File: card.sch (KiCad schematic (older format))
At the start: 25 parts, among them J1 Conn_02x03_Odd_Even, P2_FPC24/0.5MM1 Conn_01x24_Male, Q1 Si1308EDL, U1 ATMEGA168PA-AU

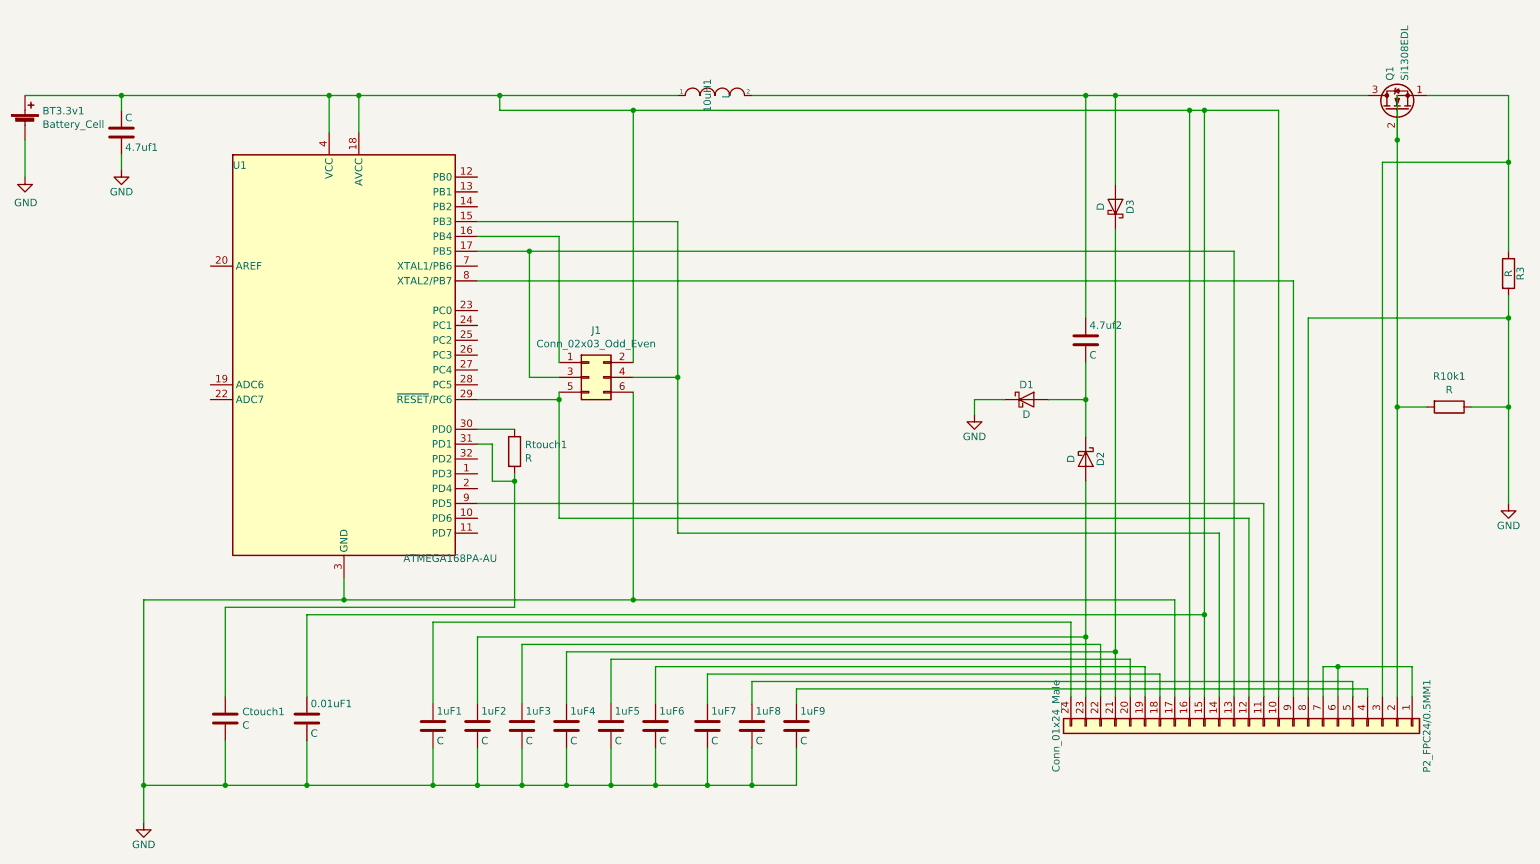
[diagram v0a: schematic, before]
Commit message: fixed FPC connector footprint, updated traces
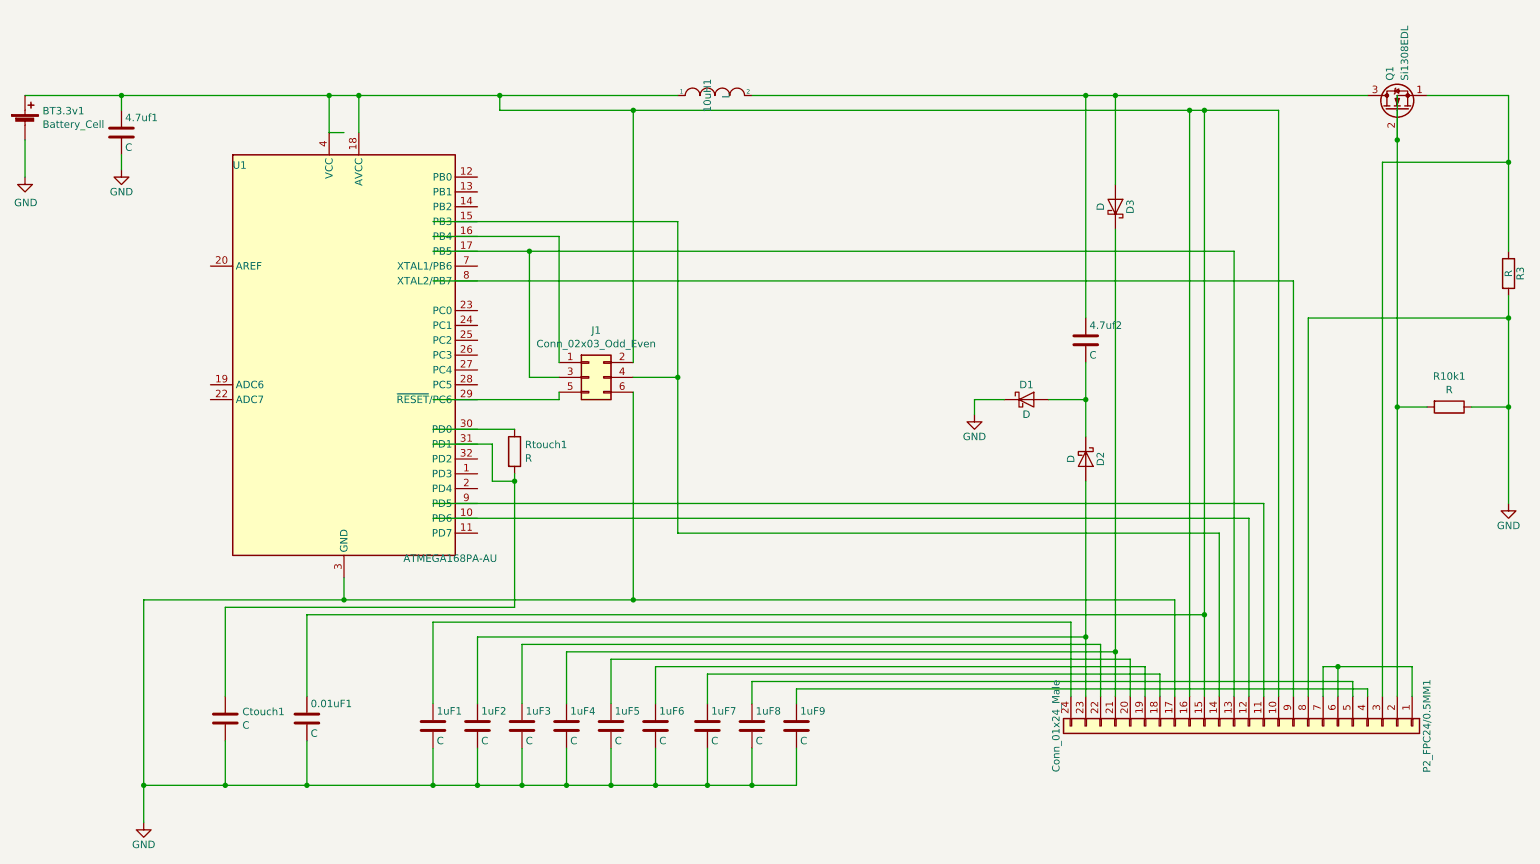
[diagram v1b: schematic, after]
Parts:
- C: renamed from 4.7uf1; value C -> 4.7uf1
- P2_FPC24/0.5MM1: footprint Connectors_FPC:Hirose_FH12-24S-0.5SH_1x24_P0.50mm_Horizontal_Gnd17 -> Connectors_FPC:Hirose_FH12-24S-0.5SH_1x24_P0.50mm_Horizontal_Gnd17_Mirr
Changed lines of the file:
@@
 F 0 "P2_FPC24/0.5MM1" H 8950 7050 50  0000 C CNN
 F 1 "Conn_01x24_Male" H 8950 4550 50  0000 C CNN
-F 2 "Connectors_FPC:Hirose_FH12-24S-0.5SH_1x24_P0.50mm_Horizontal_Gnd17" H 8950 5850 50  0001 C CNN
+F 2 "Connectors_FPC:Hirose_FH12-24S-0.5SH_1x24_P0.50mm_Horizontal_Gnd17_Mirr" H 8950 5850 50  0001 C CNN
 F 3 "" H 8950 5850 50  0001 C CNN
 	1    8950 5850
@@
 $EndComp
 $Comp
-L Device:C 4.7uf1
+L Device:C C
 U 1 1 5AB85D32
 P 1350 1850
-F 0 "4.7uf1" H 1375 1950 50  0000 L CNN
-F 1 "C" H 1375 1750 50  0000 L CNN
+F 0 "C" H 1375 1950 50  0000 L CNN
+F 1 "4.7uf1" H 1375 1750 50  0000 L CNN
 F 2 "Capacitors_SMD:C_0402" H 1388 1700 50  0001 C CNN
 F 3 "" H 1350 1850 50  0001 C CNN
@@
 	3900 1600 5100 1600
 Wire Wire Line
-	3750 2850 9250 2850
-Wire Wire Line
-	3750 4350 9050 4350
-Wire Wire Line
 	9950 1600 9950 1900
 Connection ~ 9950 1900
@@
 	4300 3600 4300 3650
 Wire Wire Line
-	4300 3650 3750 3650
-Wire Wire Line
 	4300 3400 4300 2550
 Wire Wire Line
-	4300 2550 3750 2550
-Wire Wire Line
-	3750 2450 5100 2450
-Wire Wire Line
 	5100 2450 5100 3500
 Wire Wire Line
@@
 Wire Wire Line
 	4100 3500 4100 2650
-Wire Wire Line
-	4100 2650 3750 2650
 Wire Wire Line
 	2950 1850 2950 1600
@@
 	4000 4150 4000 4200
 Wire Wire Line
-	3750 3950 3850 3950
-Wire Wire Line
 	3850 3950 3850 4200
 Wire Wire Line
@@
 	4000 4200 4000 5050
 Wire Wire Line
-	4000 3850 3750 3850
-Wire Wire Line
-	4300 3650 4300 4450
-Connection ~ 4300 3650
-Wire Wire Line
-	4300 4450 8950 4450
-Wire Wire Line
 	5100 3500 5100 4550
 Connection ~ 5100 3500
@@
 Wire Wire Line
 	4100 2650 8850 2650
+Wire Wire Line
+	2750 1850 2850 1850
+Wire Wire Line
+	3450 2450 5100 2450
+Wire Wire Line
+	3450 2550 4300 2550
+Wire Wire Line
+	3450 2650 4100 2650
+Wire Wire Line
+	3450 2850 9250 2850
+Wire Wire Line
+	3450 3650 4300 3650
+Wire Wire Line
+	3450 3850 4000 3850
+Wire Wire Line
+	3450 3950 3850 3950
+Wire Wire Line
+	3450 4350 9050 4350
+Wire Wire Line
+	3450 4450 8950 4450
 $EndSCHEMATC

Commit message: increased some footprint sizes, added missing via
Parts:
- 0.01uF1, 1uF1, 1uF2, 1uF3, 1uF4, 1uF5, 1uF6, 1uF7, 1uF8, 1uF9, 4.7uf2: footprint Capacitors_SMD:C_0402 -> Capacitors_SMD:C_0603_HandSoldering
- C1: renamed from C; footprint Capacitors_SMD:C_0402 -> Capacitors_SMD:C_0603_HandSoldering
- D1, D2, D3: footprint Diodes_SMD:D_0805 -> Diodes_SMD:D_SOD-123
- R10k1, R3, Rtouch1: footprint Resistors_SMD:R_0402 -> Resistors_SMD:R_0603_HandSoldering
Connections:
- wire segments 141 -> 143
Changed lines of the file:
@@
 F 0 "R3" V 10780 2800 50  0000 C CNN
 F 1 "R" V 10700 2800 50  0000 C CNN
-F 2 "Resistors_SMD:R_0402" V 10630 2800 50  0001 C CNN
+F 2 "Resistors_SMD:R_0603_HandSoldering" V 10630 2800 50  0001 C CNN
 F 3 "" H 10700 2800 50  0001 C CNN
 F 4 "R" H 10700 2800 50  0001 C CNN "Spice_Primitive"
@@
 F 0 "D1" H 7450 3750 50  0000 C CNN
 F 1 "D" H 7450 3550 50  0000 C CNN
-F 2 "Diodes_SMD:D_0805" H 7450 3650 50  0001 C CNN
+F 2 "Diodes_SMD:D_SOD-123" H 7450 3650 50  0001 C CNN
 F 3 "" H 7450 3650 50  0001 C CNN
 	1    7450 3650
@@
 F 0 "D2" H 7850 4150 50  0000 C CNN
 F 1 "D" H 7850 3950 50  0000 C CNN
-F 2 "Diodes_SMD:D_0805" H 7850 4050 50  0001 C CNN
+F 2 "Diodes_SMD:D_SOD-123" H 7850 4050 50  0001 C CNN
 F 3 "" H 7850 4050 50  0001 C CNN
 	1    7850 4050
@@
 F 0 "D3" H 8050 2450 50  0000 C CNN
 F 1 "D" H 8050 2250 50  0000 C CNN
-F 2 "Diodes_SMD:D_0805" H 8050 2350 50  0001 C CNN
+F 2 "Diodes_SMD:D_SOD-123" H 8050 2350 50  0001 C CNN
 F 3 "" H 8050 2350 50  0001 C CNN
 	1    8050 2350
@@
 F 0 "4.7uf2" H 7875 3350 50  0000 L CNN
 F 1 "C" H 7875 3150 50  0000 L CNN
-F 2 "Capacitors_SMD:C_0402" H 7888 3100 50  0001 C CNN
+F 2 "Capacitors_SMD:C_0603_HandSoldering" H 7888 3100 50  0001 C CNN
 F 3 "" H 7850 3250 50  0001 C CNN
 	1    7850 3250
@@
 $EndComp
 $Comp
-L Device:C C
+L Device:C C1
 U 1 1 5AB85D32
 P 1350 1850
-F 0 "C" H 1375 1950 50  0000 L CNN
+F 0 "C1" H 1375 1950 50  0000 L CNN
 F 1 "4.7uf1" H 1375 1750 50  0000 L CNN
-F 2 "Capacitors_SMD:C_0402" H 1388 1700 50  0001 C CNN
+F 2 "Capacitors_SMD:C_0603_HandSoldering" H 1388 1700 50  0001 C CNN
 F 3 "" H 1350 1850 50  0001 C CNN
 	1    1350 1850
@@
 F 0 "1uF3" H 4075 5950 50  0000 L CNN
 F 1 "C" H 4075 5750 50  0000 L CNN
-F 2 "Capacitors_SMD:C_0402" H 4088 5700 50  0001 C CNN
+F 2 "Capacitors_SMD:C_0603_HandSoldering" H 4088 5700 50  0001 C CNN
 F 3 "" H 4050 5850 50  0001 C CNN
 	1    4050 5850
@@
 F 0 "1uF4" H 4375 5950 50  0000 L CNN
 F 1 "C" H 4375 5750 50  0000 L CNN
-F 2 "Capacitors_SMD:C_0402" H 4388 5700 50  0001 C CNN
+F 2 "Capacitors_SMD:C_0603_HandSoldering" H 4388 5700 50  0001 C CNN
 F 3 "" H 4350 5850 50  0001 C CNN
 	1    4350 5850
@@
 F 0 "1uF5" H 4675 5950 50  0000 L CNN
 F 1 "C" H 4675 5750 50  0000 L CNN
-F 2 "Capacitors_SMD:C_0402" H 4688 5700 50  0001 C CNN
+F 2 "Capacitors_SMD:C_0603_HandSoldering" H 4688 5700 50  0001 C CNN
 F 3 "" H 4650 5850 50  0001 C CNN
 	1    4650 5850
@@
 F 0 "1uF6" H 4975 5950 50  0000 L CNN
 F 1 "C" H 4975 5750 50  0000 L CNN
-F 2 "Capacitors_SMD:C_0402" H 4988 5700 50  0001 C CNN
+F 2 "Capacitors_SMD:C_0603_HandSoldering" H 4988 5700 50  0001 C CNN
 F 3 "" H 4950 5850 50  0001 C CNN
 	1    4950 5850
@@
 F 0 "1uF7" H 5325 5950 50  0000 L CNN
 F 1 "C" H 5325 5750 50  0000 L CNN
-F 2 "Capacitors_SMD:C_0402" H 5338 5700 50  0001 C CNN
+F 2 "Capacitors_SMD:C_0603_HandSoldering" H 5338 5700 50  0001 C CNN
 F 3 "" H 5300 5850 50  0001 C CNN
 	1    5300 5850
@@
 F 0 "1uF8" H 5625 5950 50  0000 L CNN
 F 1 "C" H 5625 5750 50  0000 L CNN
-F 2 "Capacitors_SMD:C_0402" H 5638 5700 50  0001 C CNN
+F 2 "Capacitors_SMD:C_0603_HandSoldering" H 5638 5700 50  0001 C CNN
 F 3 "" H 5600 5850 50  0001 C CNN
 	1    5600 5850
@@
 F 0 "1uF2" H 3775 5950 50  0000 L CNN
 F 1 "C" H 3775 5750 50  0000 L CNN
-F 2 "Capacitors_SMD:C_0402" H 3788 5700 50  0001 C CNN
+F 2 "Capacitors_SMD:C_0603_HandSoldering" H 3788 5700 50  0001 C CNN
 F 3 "" H 3750 5850 50  0001 C CNN
 	1    3750 5850
@@
 F 0 "1uF1" H 3475 5950 50  0000 L CNN
 F 1 "C" H 3475 5750 50  0000 L CNN
-F 2 "Capacitors_SMD:C_0402" H 3488 5700 50  0001 C CNN
+F 2 "Capacitors_SMD:C_0603_HandSoldering" H 3488 5700 50  0001 C CNN
 F 3 "" H 3450 5850 50  0001 C CNN
 	1    3450 5850
@@
 F 0 "1uF9" H 5925 5950 50  0000 L CNN
 F 1 "C" H 5925 5750 50  0000 L CNN
-F 2 "Capacitors_SMD:C_0402" H 5938 5700 50  0001 C CNN
+F 2 "Capacitors_SMD:C_0603_HandSoldering" H 5938 5700 50  0001 C CNN
 F 3 "" H 5900 5850 50  0001 C CNN
 	1    5900 5850
@@
 Connection ~ 10700 3100
 Wire Wire Line
-	9250 5650 9250 2850
+	9250 5650 9250 4700
 Wire Wire Line
 	9150 5650 9150 1700
@@
 F 0 "0.01uF1" H 2625 5900 50  0000 L CNN
 F 1 "C" H 2625 5700 50  0000 L CNN
-F 2 "Capacitors_SMD:C_0402" H 2638 5650 50  0001 C CNN
+F 2 "Capacitors_SMD:C_0603_HandSoldering" H 2638 5650 50  0001 C CNN
 F 3 "" H 2600 5800 50  0001 C CNN
 F 4 "C" H 2600 5800 50  0001 C CNN "Spice_Primitive"
@@
 F 0 "R10k1" V 10093 3700 50  0000 C CNN
 F 1 "R" V 10184 3700 50  0000 C CNN
-F 2 "Resistors_SMD:R_0402" V 10230 3700 50  0001 C CNN
+F 2 "Resistors_SMD:R_0603_HandSoldering" V 10230 3700 50  0001 C CNN
 F 3 "~" H 10300 3700 50  0001 C CNN
 F 4 "R" H 10300 3700 50  0001 C CNN "Spice_Primitive"
@@
 F 0 "Rtouch1" H 4070 4046 50  0000 L CNN
 F 1 "R" H 4070 3955 50  0000 L CNN
-F 2 "Resistors_SMD:R_0402" V 3930 4000 50  0001 C CNN
+F 2 "Resistors_SMD:R_0603_HandSoldering" V 3930 4000 50  0001 C CNN
 F 3 "~" H 4000 4000 50  0001 C CNN
 	1    4000 4000
@@
 	3450 2650 4100 2650
 Wire Wire Line
-	3450 2850 9250 2850
-Wire Wire Line
 	3450 3650 4300 3650
 Wire Wire Line
@@
 Wire Wire Line
 	3450 4450 8950 4450
+Wire Wire Line
+	3450 4550 4950 4550
+Wire Wire Line
+	4950 4550 4950 4700
+Wire Wire Line
+	4950 4700 9250 4700
 $EndSCHEMATC

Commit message: Connected display reset to AVR, increased inductor footprint size.
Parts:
- 10uH1: footprint Inductors_SMD:L_0805 -> Inductors_SMD:L_1210_HandSoldering
- Q1: footprint TO_SOT_Packages_SMD:SOT-223 -> TO_SOT_Packages_SMD:SOT-323_SC-70_Handsoldering
- Rtouch1: value R -> 1M
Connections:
- net labels added: BS, BUSY, CS, DC, GDR, PREVGH, PREVGL, RES, RESE, SCLK, SDI
- wire segments 143 -> 145
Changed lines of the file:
@@
 F 0 "Q1" H 10150 1750 50  0000 L CNN
 F 1 "Si1308EDL" H 10150 1650 50  0000 L CNN
-F 2 "TO_SOT_Packages_SMD:SOT-223" H 10150 1800 50  0001 C CNN
+F 2 "TO_SOT_Packages_SMD:SOT-323_SC-70_Handsoldering" H 10150 1800 50  0001 C CNN
 F 3 "" H 9950 1700 50  0001 C CNN
 	1    9950 1700
@@
 F 0 "10uH1" V 5300 1600 50  0000 C CNN
 F 1 "L" V 5425 1600 50  0000 C CNN
-F 2 "Inductors_SMD:L_0805" H 5350 1600 50  0001 C CNN
+F 2 "Inductors_SMD:L_1210_HandSoldering" H 5350 1600 50  0001 C CNN
 F 3 "" H 5350 1600 50  0001 C CNN
 	1    5350 1600
@@
 	9250 5650 9250 4700
 Wire Wire Line
-	9150 5650 9150 1700
-Wire Wire Line
-	9150 1700 8650 1700
+	9150 5650 9150 2750
 Wire Wire Line
 	9050 5650 9050 4350
@@
 Wire Wire Line
 	8650 1700 8650 5100
-Connection ~ 8650 1700
 Connection ~ 8650 5100
 Wire Wire Line
@@
 P 4000 4000
 F 0 "Rtouch1" H 4070 4046 50  0000 L CNN
-F 1 "R" H 4070 3955 50  0000 L CNN
+F 1 "1M" H 4070 3955 50  0000 L CNN
 F 2 "Resistors_SMD:R_0603_HandSoldering" V 3930 4000 50  0001 C CNN
 F 3 "~" H 4000 4000 50  0001 C CNN
@@
 Wire Wire Line
 	4950 4700 9250 4700
+Wire Wire Line
+	3450 3250 3750 3250
+Wire Wire Line
+	3750 3250 3750 2750
+Wire Wire Line
+	3750 2750 9150 2750
+Text Label 8950 2750 0    50   ~ 0
+RES
+Text Label 9950 2350 0    50   ~ 0
+GDR
+Text Label 10300 2050 0    50   ~ 0
+RESE
+Text Label 9500 3100 0    50   ~ 0
+BS
+Text Label 6850 4700 0    50   ~ 0
+BUSY
+Text Label 6450 4350 0    50   ~ 0
+DC
+Text Label 6600 4450 0    50   ~ 0
+CS
+Text Label 6500 2650 0    50   ~ 0
+SCLK
+Text Label 6750 4550 0    50   ~ 0
+SDI
+Text Label 7850 4950 0    50   ~ 0
+PREVGL
+Text Label 8050 4800 0    50   ~ 0
+PREVGH
 $EndSCHEMATC
